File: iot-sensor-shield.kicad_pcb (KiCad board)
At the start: 2 copper layers, 68.5 x 53.3 mm, 4 parts, among them P1 CONN_01X10, P2 CONN_01X06, P3 CONN_01X08, P4 CONN_01X08

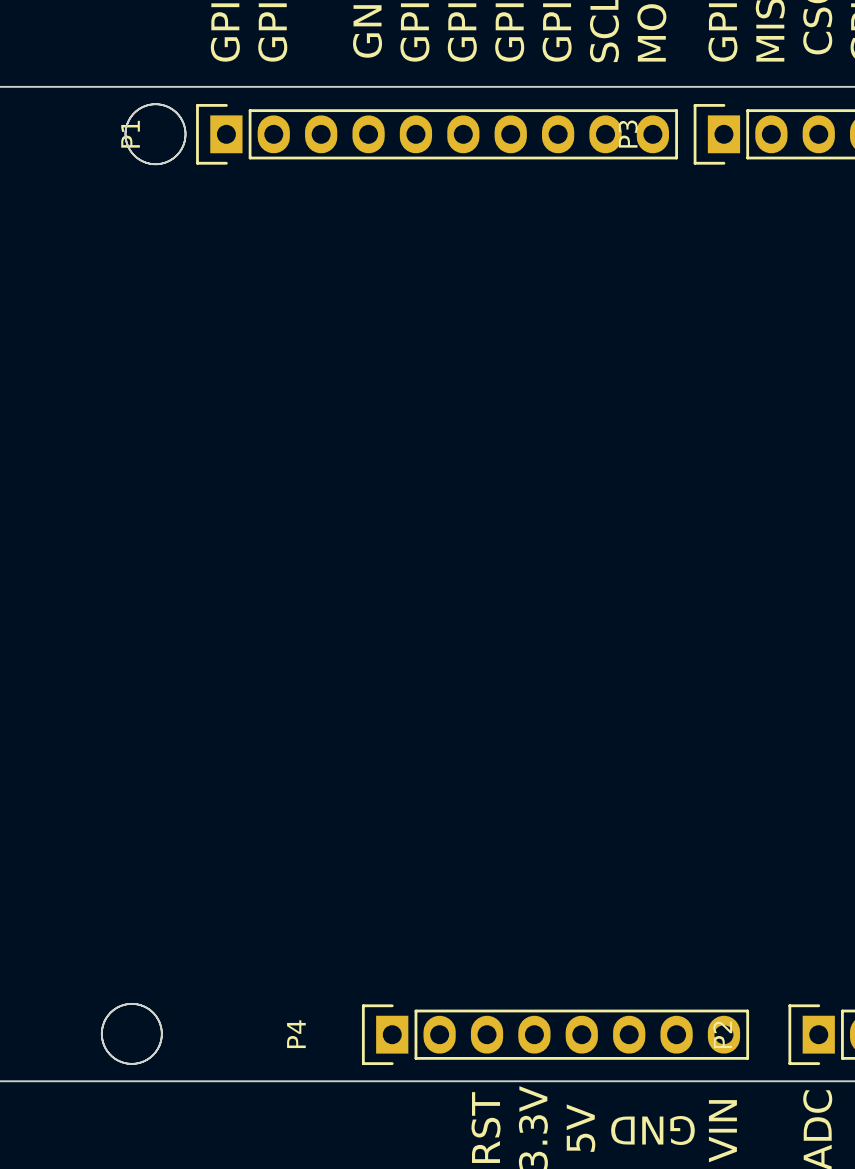
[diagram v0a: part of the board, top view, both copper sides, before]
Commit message: add led GPIO16 & button GPIO0
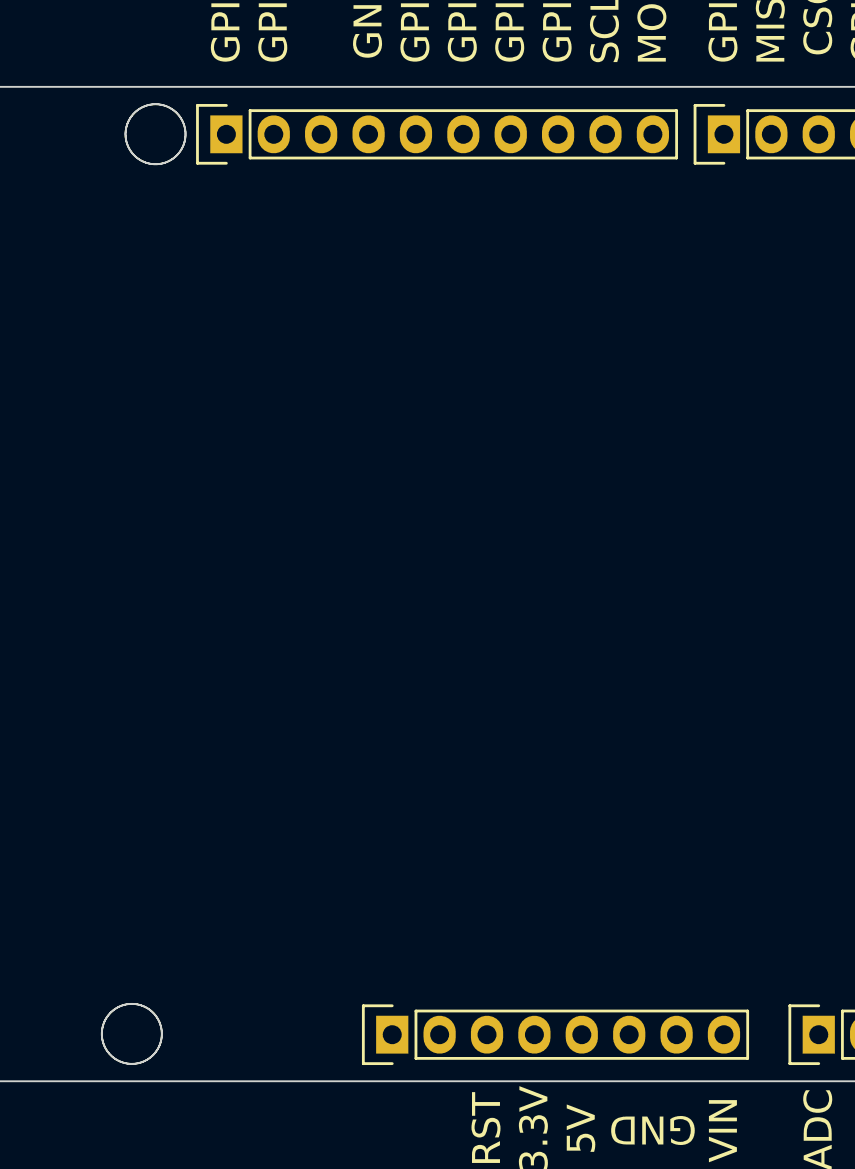
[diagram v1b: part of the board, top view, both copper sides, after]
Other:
- board text removed: "53.3000"
- board text removed: "68.5346"
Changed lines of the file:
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@@
-(kicad_pcb (version 20160815) (host pcbnew 201611221049+7374~55~ubuntu16.04.1-product)
+(kicad_pcb (version 20160815) (host pcbnew no-vcs-found-7397~56~ubuntu16.04.1)
   (general
     (links 0)
     (no_connects 0)
-    (area 112.902236 44.141504 228.896298 104.111917)
+    (area 109.186452 71.065504 177.821071 124.465506)
     (thickness 1.6)
-    (drawings 780)
+    (drawings 778)
     (tracks 0)
     (zones 0)
@@
     (descr "Through hole pin header")
     (tags "pin header")
-    (fp_text reference P1 (at 0 -5.1 90) (layer F.SilkS)
+    (fp_text reference P1 (at 0 -5.1 90) (layer F.SilkS) hide
       (effects (font (size 1 1) (thickness 0.15)))
     )
-    (fp_text value CONN_01X10 (at 0 -3.1 90) (layer F.Fab)
+    (fp_text value CONN_01X10 (at 0 -3.1 90) (layer F.Fab) hide
       (effects (font (size 1 1) (thickness 0.15)))
     )
@@
     (pad 1 thru_hole rect (at 0 0 90) (size 2.032 1.7272) (drill 1.016) (layers *.Cu *.Mask))
     (model Pin_Headers.3dshapes/Pin_Header_Straight_1x10.wrl
-      (at (xyz 0 -0.45 0))
+      (at (xyz 0 -0.45 -0.07874015748031496))
       (scale (xyz 1 1 1))
-      (rotate (xyz 0 0 90))
+      (rotate (xyz 0 180 90))
     )
   )
@@
     (descr "Through hole pin header")
     (tags "pin header")
-    (fp_text reference P2 (at 0 -5.1 90) (layer F.SilkS)
+    (fp_text reference P2 (at 0 -5.1 90) (layer F.SilkS) hide
       (effects (font (size 1 1) (thickness 0.15)))
     )
-    (fp_text value CONN_01X06 (at 0 -3.1 90) (layer F.Fab)
+    (fp_text value CONN_01X06 (at 0 -3.1 90) (layer F.Fab) hide
       (effects (font (size 1 1) (thickness 0.15)))
     )
@@
     (pad 1 thru_hole rect (at 0 0 90) (size 2.032 1.7272) (drill 1.016) (layers *.Cu *.Mask))
     (model Pin_Headers.3dshapes/Pin_Header_Straight_1x06.wrl
-      (at (xyz 0 -0.25 0))
+      (at (xyz 0 -0.25 -0.07874015748031496))
       (scale (xyz 1 1 1))
-      (rotate (xyz 0 0 90))
+      (rotate (xyz 0 180 90))
     )
   )
@@
     (descr "Through hole pin header")
     (tags "pin header")
-    (fp_text reference P3 (at 0 -5.1 90) (layer F.SilkS)
+    (fp_text reference P3 (at 0 -5.1 90) (layer F.SilkS) hide
       (effects (font (size 1 1) (thickness 0.15)))
     )
-    (fp_text value CONN_01X08 (at 0 -3.1 90) (layer F.Fab)
+    (fp_text value CONN_01X08 (at 0 -3.1 90) (layer F.Fab) hide
       (effects (font (size 1 1) (thickness 0.15)))
     )
@@
     (pad 1 thru_hole rect (at 0 0 90) (size 2.032 1.7272) (drill 1.016) (layers *.Cu *.Mask))
     (model Pin_Headers.3dshapes/Pin_Header_Straight_1x08.wrl
-      (at (xyz 0 -0.35 0))
+      (at (xyz 0 -0.35 -0.07874015748031496))
       (scale (xyz 1 1 1))
-      (rotate (xyz 0 0 90))
+      (rotate (xyz 0 180 90))
     )
   )
@@
     (descr "Through hole pin header")
     (tags "pin header")
-    (fp_text reference P4 (at 0 -5.1 90) (layer F.SilkS)
+    (fp_text reference P4 (at 0 -5.1 90) (layer F.SilkS) hide
       (effects (font (size 1 1) (thickness 0.15)))
     )
-    (fp_text value CONN_01X08 (at 0 -3.1 90) (layer F.Fab)
+    (fp_text value CONN_01X08 (at 0 -3.1 90) (layer F.Fab) hide
       (effects (font (size 1 1) (thickness 0.15)))
     )
@@
     (pad 8 thru_hole oval (at 0 17.78 90) (size 2.032 1.7272) (drill 1.016) (layers *.Cu *.Mask))
     (model Pin_Headers.3dshapes/Pin_Header_Straight_1x08.wrl
-      (at (xyz 0 -0.35 0))
+      (at (xyz 0 -0.35 -0.07874015748031496))
       (scale (xyz 1 1 1))
-      (rotate (xyz 0 0 90))
+      (rotate (xyz 0 180 90))
     )
   )
@@
   (gr_line (start 125.323232 75.018352) (end 125.370307 74.987782) (layer Edge.Cuts) (width 0.1))
   (gr_line (start 176.703046 116.148651) (end 176.679661 116.098079) (layer Edge.Cuts) (width 0.1))
-  (gr_text 68.5346 (at 143.503761 130.805916) (layer Edge.Cuts)
-    (effects (font (size 0.18 0.144) (thickness 0.1)))
-  )
   (gr_line (start 125.671902 72.585036) (end 125.634128 72.544078) (layer Edge.Cuts) (width 0.1))
   (gr_line (start 125.708235 72.627279) (end 125.671902 72.585036) (layer Edge.Cuts) (width 0.1))
@@
   (gr_line (start 125.285819 72.268186) (end 125.2373 72.240793) (layer Edge.Cuts) (width 0.1))
   (gr_line (start 125.333359 72.297243) (end 125.285819 72.268186) (layer Edge.Cuts) (width 0.1))
-  (gr_text 53.3000 (at 103.480237 97.765505) (layer Edge.Cuts)
-    (effects (font (size 0.18 0.144) (thickness 0.1)))
-  )
   (gr_line (start 124.860104 75.214939) (end 124.914322 75.200411) (layer Edge.Cuts) (width 0.1))
   (gr_line (start 176.679661 88.189107) (end 176.654537 88.139375) (layer Edge.Cuts) (width 0.1))
